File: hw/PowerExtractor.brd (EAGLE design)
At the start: 75.9 x 82.5 mm, 86 parts, among them IC1 LM358D, Q1 BSS84, Q2 IRL530, Q4 BC847SMD, Q7 IRF530, T1 IRL530N, T2 IRF7416, U1 ZXCT1086E5TA, U2 ZXCT1086E5TA

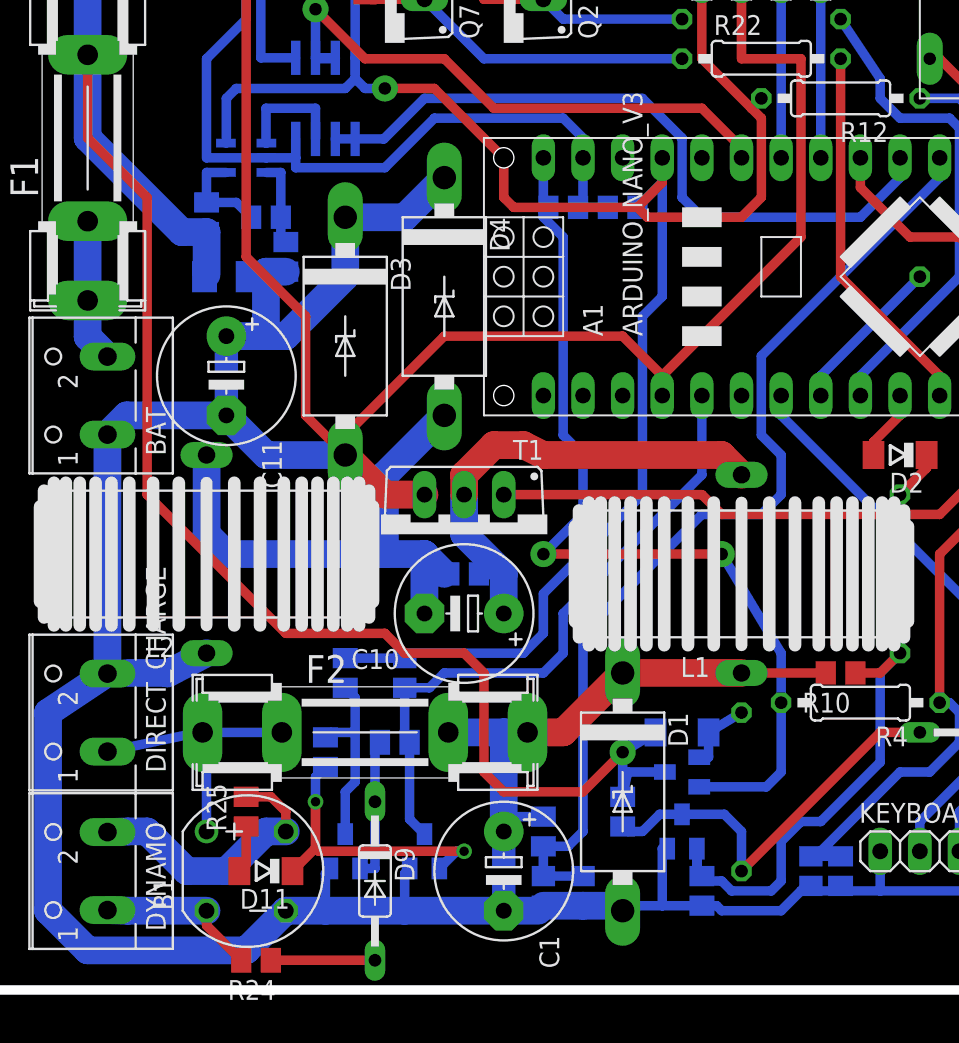
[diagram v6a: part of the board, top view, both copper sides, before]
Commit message: Shifted speed sense circuit under MCU
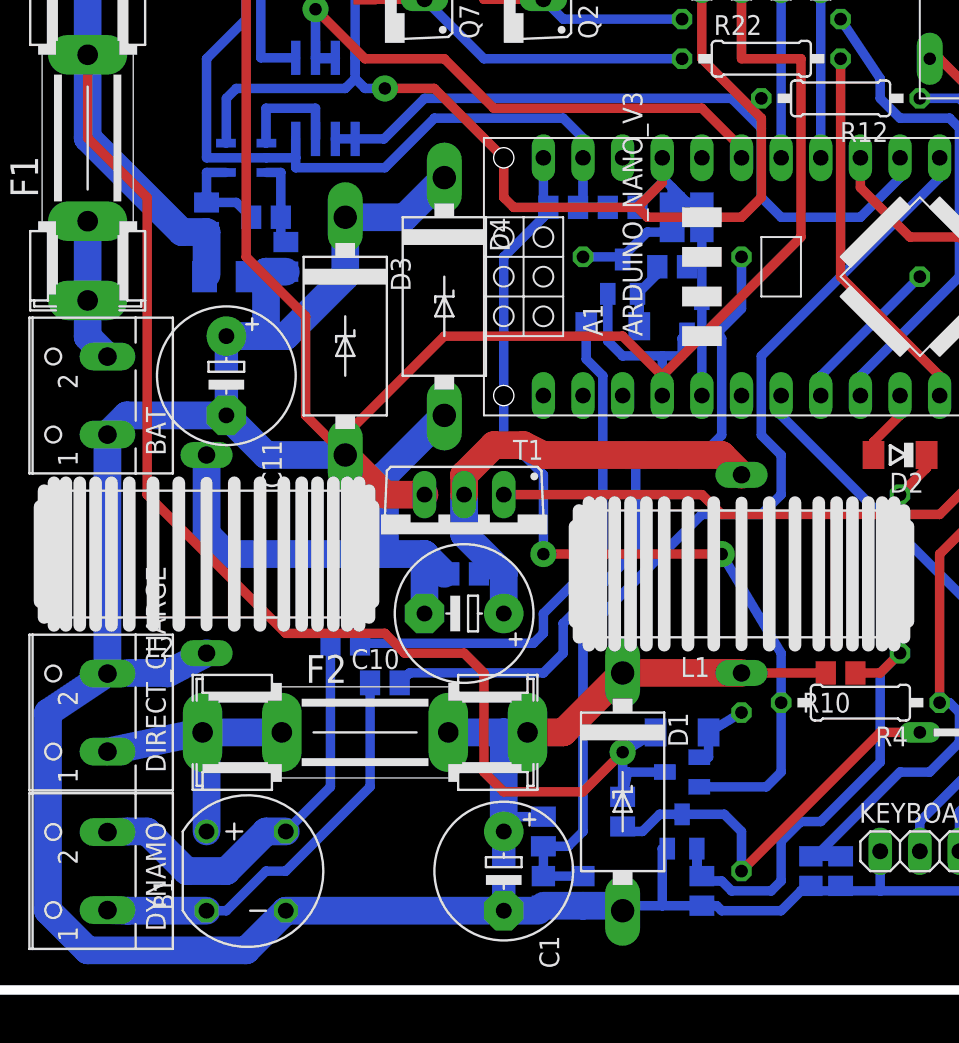
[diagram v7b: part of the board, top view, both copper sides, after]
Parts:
- D9: value 1N4148DO35-10 -> 1N4148MINIMELF; device triakcz:DO35-10 -> triakcz:SOD80C
- R26: device rcl:M0805 -> rcl:R0805
- R8: device rcl:M0805 -> rcl:0207/10
- moved U$3 40.9 mm to (39.4, 44.5)
- moved D9 38.7 mm to (38.7, 41.3), flipped to the bottom, turned to 0 degrees
- moved U$2 38.6 mm to (44.5, 41.9)
- moved R8 38.4 mm to (41.9, 45.7), turned to 0 degrees
- moved D11 36.8 mm to (41.9, 33.0), flipped to the bottom, turned to 0 degrees
- moved R29 35.9 mm to (42.5, 48.3)
- moved R26 35.3 mm to (42.5, 45.1)
- moved R28 34.9 mm to (44.5, 48.3)
- moved R24 21.1 mm to (21.6, 21.0), flipped to the bottom, turned to 0 degrees
- moved R25 12.1 mm to (24.1, 18.4), flipped to the bottom, turned to 0 degrees
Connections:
- removed net HUB_1: B1.AC2, DYNAMO.1, R24.2
- new net HUB1: B1.AC2, DYNAMO.1, R25.2
- net HUB2: now also R24.2; no longer R25.2
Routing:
- net +5V: track 129.5 -> 86.6 mm
- net ARDUINO_ROTATION_INT: track 41.2 -> 11.7 mm
- net N$29: track 6.67 -> 33.7 mm
- net HUB1: track 0.00 -> 26.8 mm
- net N$38: track 3.04 -> 25.9 mm
- net HUB_1: track 10.4 -> 0.00 mm
- net HUB2: track 17.7 -> 26.8 mm
- net GND: track 383.1 -> 389.7 mm
- net N$30: track 11.9 -> 6.37 mm
- net N$31: track 9.17 -> 4.39 mm
- net N$32: track 19.2 -> 14.9 mm, vias 2 -> 0

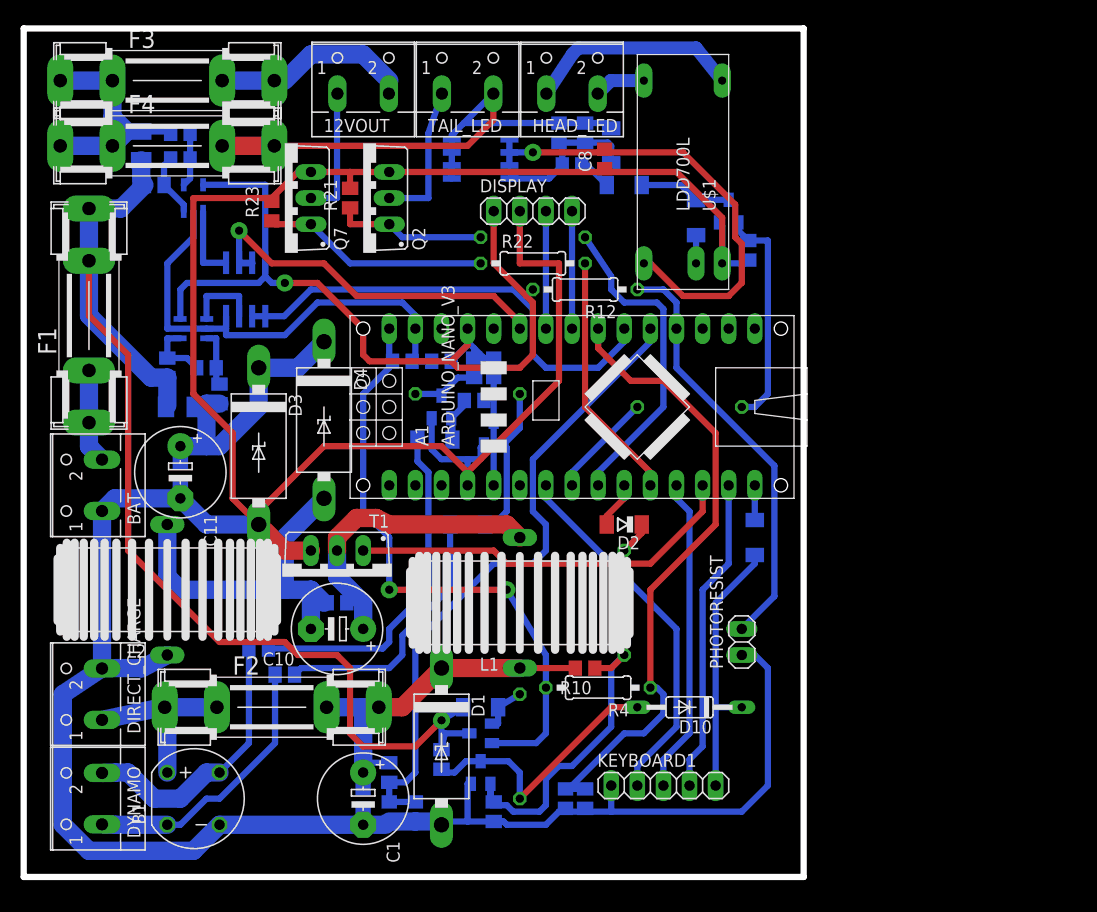
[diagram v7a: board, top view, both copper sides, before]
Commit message: Refactored PCB layout
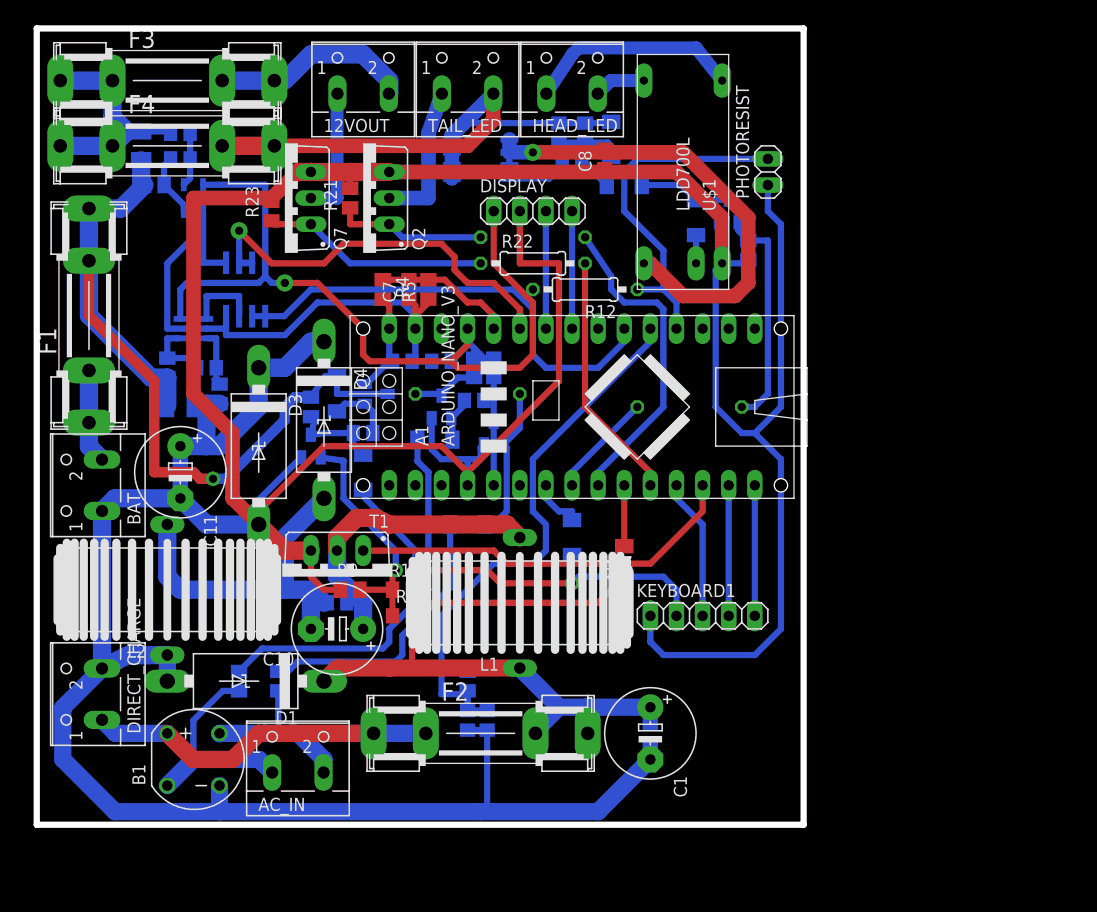
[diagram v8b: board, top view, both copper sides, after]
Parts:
- removed DYNAMO: (no value), con-wago-500:W237-102
- added AC_IN: (no value), con-wago-500:W237-102
- D10: value 1N4148DO35-10 -> 1N4148MINIMELF; device triakcz:DO35-10 -> triakcz:SOD80C
- R11, R4, R6: device rcl:0207/10 -> rcl:M0805
- moved C7 51.8 mm to (36.2, 55.9), flipped to the top
- moved R5 51.8 mm to (38.1, 55.9), flipped to the top
- moved PHOTORESIST 45.8 mm to (71.1, 67.3)
- moved R4 44.0 mm to (33.7, 55.9), turned to 270 degrees
- moved D10 39.1 mm to (31.8, 38.1), flipped to the bottom, turned to 90 degrees
- moved R3 36.6 mm to (26.7, 44.5)
- moved U$4 35.8 mm to (26.7, 40.6)
- moved Q1 34.5 mm to (33.0, 45.7), turned to 90 degrees
- moved R6 34.1 mm to (31.8, 41.9), turned to 0 degrees
- moved D6 33.5 mm to (29.2, 45.7), turned to 270 degrees
- moved C1 28.7 mm to (59.7, 12.7)
- moved C2 28.7 mm to (59.7, 12.7)
- moved R9 25.7 mm to (30.5, 26.7), flipped to the top, turned to 0 degrees
- moved R11 21.6 mm to (35.6, 26.7), flipped to the top, turned to 0 degrees
- moved F2 20.5 mm to (43.2, 12.7)
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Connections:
- removed net N$36: D10.C, D12.C, KEYBOARD1.5
- new net N$41: A1.D4, D12.A
- net ARDUINO_VOUT_SENSE: now also A1.A7; no longer A1.A3
- net HUB1: now also AC_IN.1, R24.2; no longer DYNAMO.1, R25.2
- net HUB2: now also AC_IN.2, R25.2; no longer DYNAMO.2, R24.2
- net N$39: now also KEYBOARD1.5; no longer D12.A
- net N$6: now also D10.C, D12.C; no longer A1.D4
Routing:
- net GND: track 389.7 -> 465.9 mm
- net ARDUINO_VIN: track 60.1 -> 9.91 mm, vias 2 -> 0
- net ARDUINO_VOUT_SENSE: track 62.6 -> 13.5 mm
- net BAT+FUSED: track 117.3 -> 85.3 mm
- net N$36: track 26.5 -> 0.00 mm
- net N$12: track 3.24 -> 22.0 mm
- net N$37: track 30.8 -> 12.7 mm
- net N$22: track 26.3 -> 8.54 mm
- net VIN: track 37.2 -> 54.3 mm
- net N$26: track 30.8 -> 13.8 mm
- net N$10: track 17.8 -> 34.1 mm
- net ARDUINO_VIN_ANALOG: track 63.3 -> 53.9 mm
- net N$39: track 3.38 -> 12.7 mm
- net N$4: track 31.8 -> 22.8 mm, vias 0 -> 1
- net HUB2: track 26.8 -> 17.8 mm
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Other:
- board size 75.9 x 82.5 mm -> 74.6 x 77.5 mm
